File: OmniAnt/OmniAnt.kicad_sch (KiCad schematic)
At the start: 43 parts, among them J1 Connector, USB-TYPE-C-16P, J14 Conn_01x01, J15 Conn_01x01, J16 Conn_01x01, J17 Conn_01x01, J18 Conn_01x01, J19 Conn_01x01, J2 Conn_01x02_Pin, J20 Conn_01x01, J21 Conn_01x01, J22 Conn_01x01, J24 Conn_01x01, J3 Conn_01x04_Pin, J4 XT30PW-M, J5 XT30PW-M, J6 XT30PW-M, J7 XT30PW-M, U1 USBLC6-2P6, U2 TPSM53603RDA, U3 ESP32-S3-WROOM-1

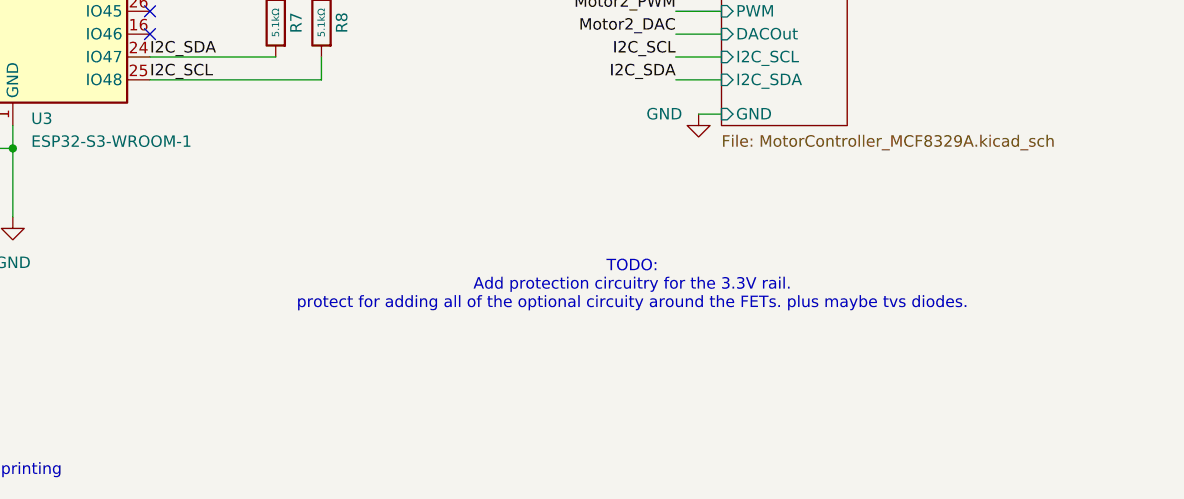
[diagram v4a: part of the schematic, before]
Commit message: Ok I did a lot of reading today. I'm going to split each FET into a sheet, so I can add the external circuitry more easily.
I may need to source a different FET. The one I selected has a good EAS, but the rating is only for 11A. and Ideally I would be able to do 19 or 20A. I'm sure I will never do that much current , but relying on the mosfet to handle things seems better than adding an additional tvs diode. Snubber is the way to go for sure to keep things cool.
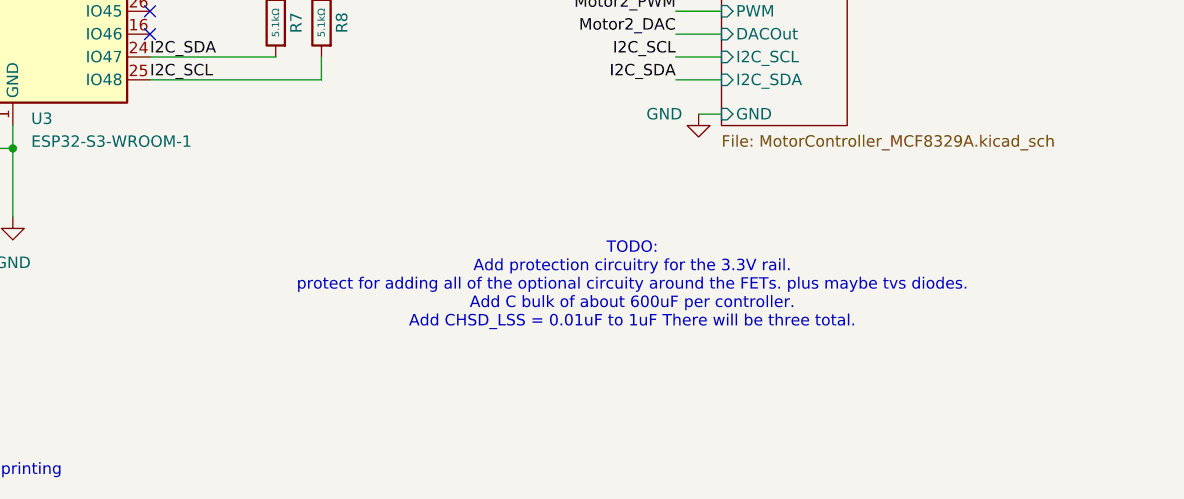
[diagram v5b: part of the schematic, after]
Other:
- note added: "TODO: Add protection circuitry for the 3.3V rail. protect for adding all of the optional circuity around the FETs. plus maybe tvs diodes. Add C bulk of about 600uF per controller. Add CHSD_LSS = 0.01uF to 1uF There will be three total."
- note removed: "TODO: Add protection circuitry for the 3.3V rail. protect for adding all of the optional circuity around the FETs. plus maybe tvs diodes."
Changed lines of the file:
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@@
 	(generator_version "9.0")
 	(paper "A4")
-	(text "TODO:\nAdd protection circuitry for the 3.3V rail. \nprotect for adding all of the optional circuity around the FETs. plus maybe tvs diodes. \n"
+	(text "TODO:\nAdd protection circuitry for the 3.3V rail. \nprotect for adding all of the optional circuity around the FETs. plus maybe tvs diodes. \nAdd C bulk of about 600uF per controller. \nAdd CHSD_LSS = 0.01uF to 1uF There will be three total. "
 		(exclude_from_sim yes)
 		(at 225.044 172.72 0)

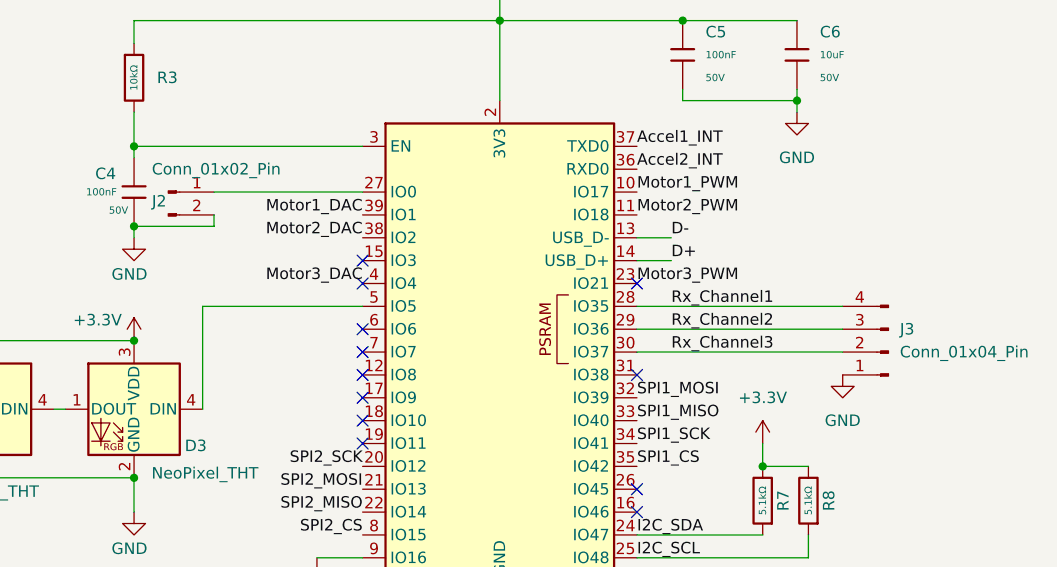
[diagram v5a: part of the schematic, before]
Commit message: I got the mosfets in as a separate sheet and selected the additional protection circuitry. I'm working on finding the other recommended capacitors now.
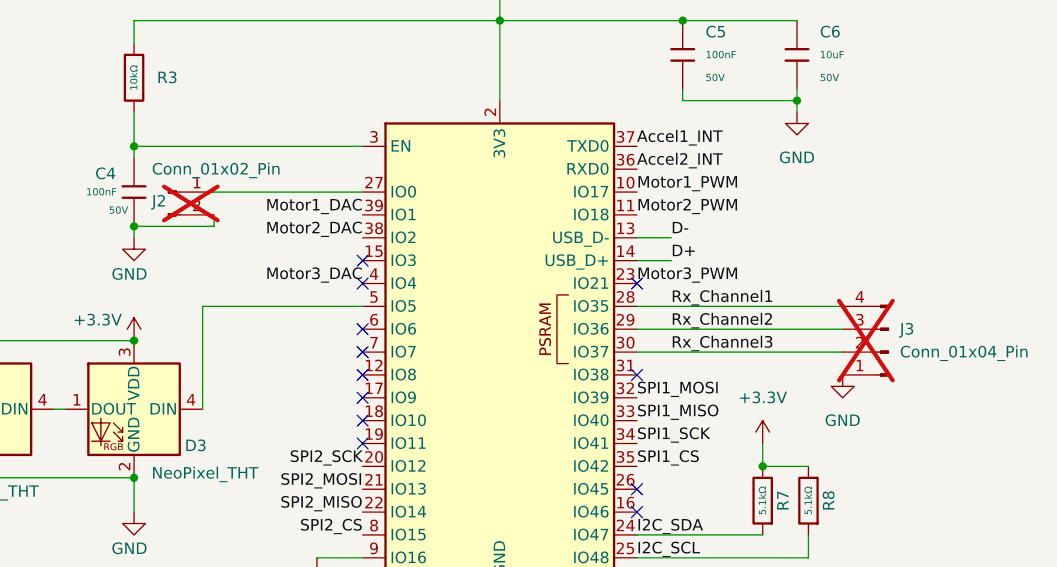
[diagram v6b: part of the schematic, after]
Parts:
- J2, J3: now not fitted
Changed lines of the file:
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@@
 		(in_bom yes)
 		(on_board yes)
-		(dnp no)
+		(dnp yes)
 		(fields_autoplaced yes)
 		(property "Reference" "J3"
@@
 		(in_bom yes)
 		(on_board yes)
-		(dnp no)
+		(dnp yes)
 		(property "Reference" "J2"
 			(at 118.364 110.236 0)

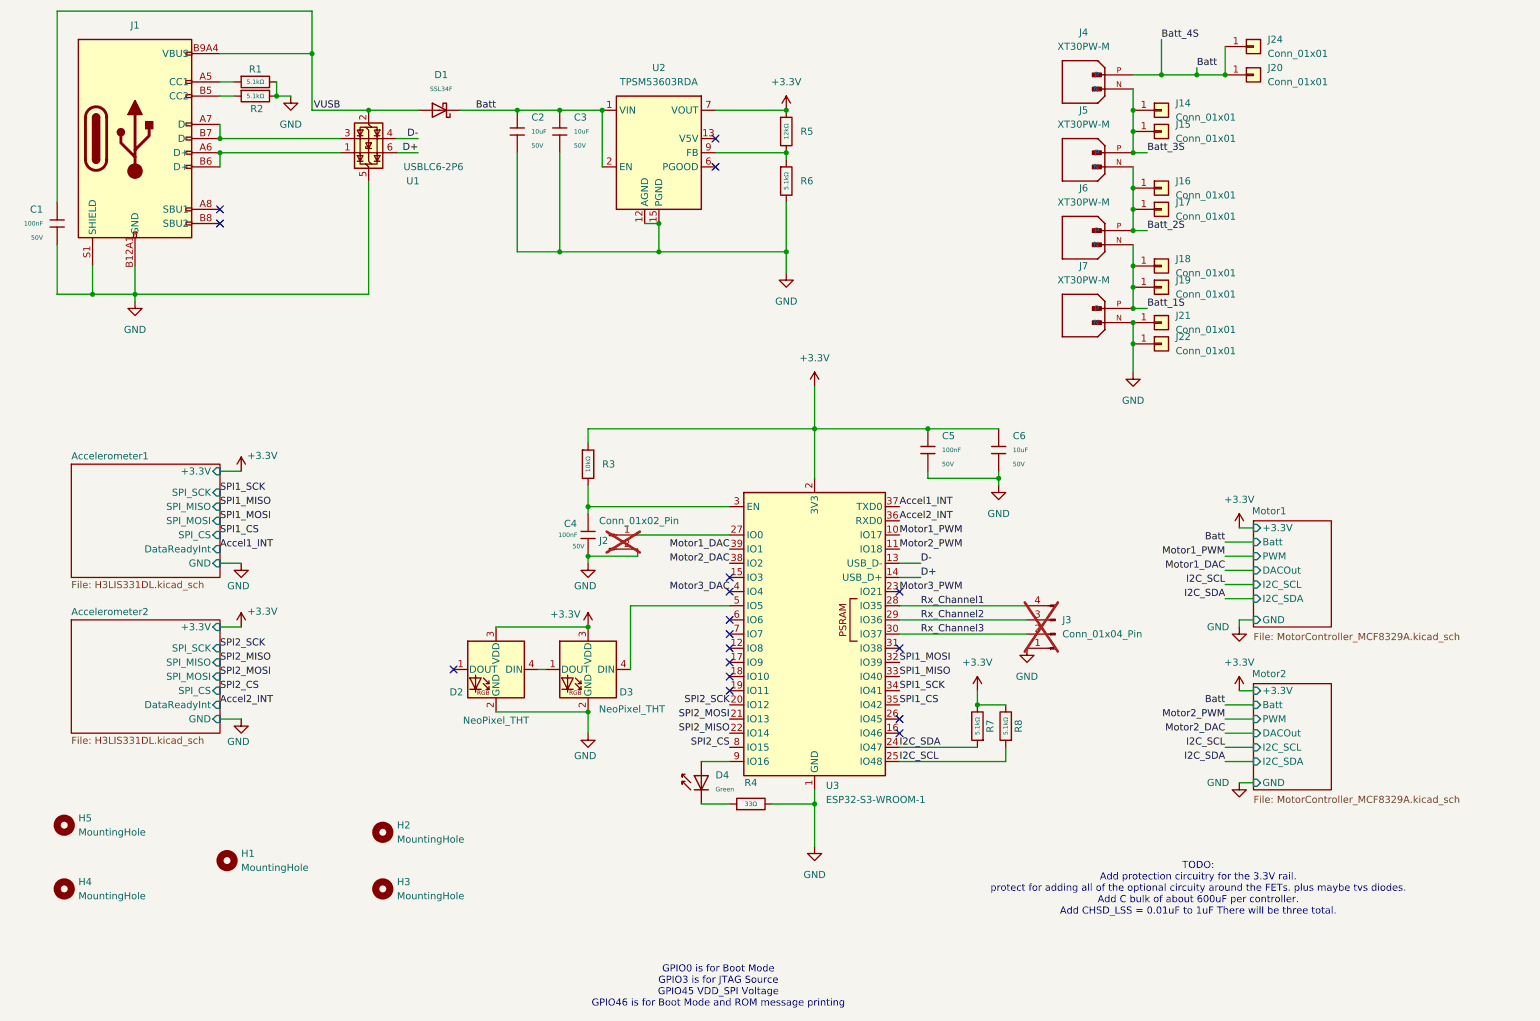
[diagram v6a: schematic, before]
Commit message: Well shit making the FETs into libraries totally screwed up the annotation :( I decided to just redo the layout for the FETs anyhow.
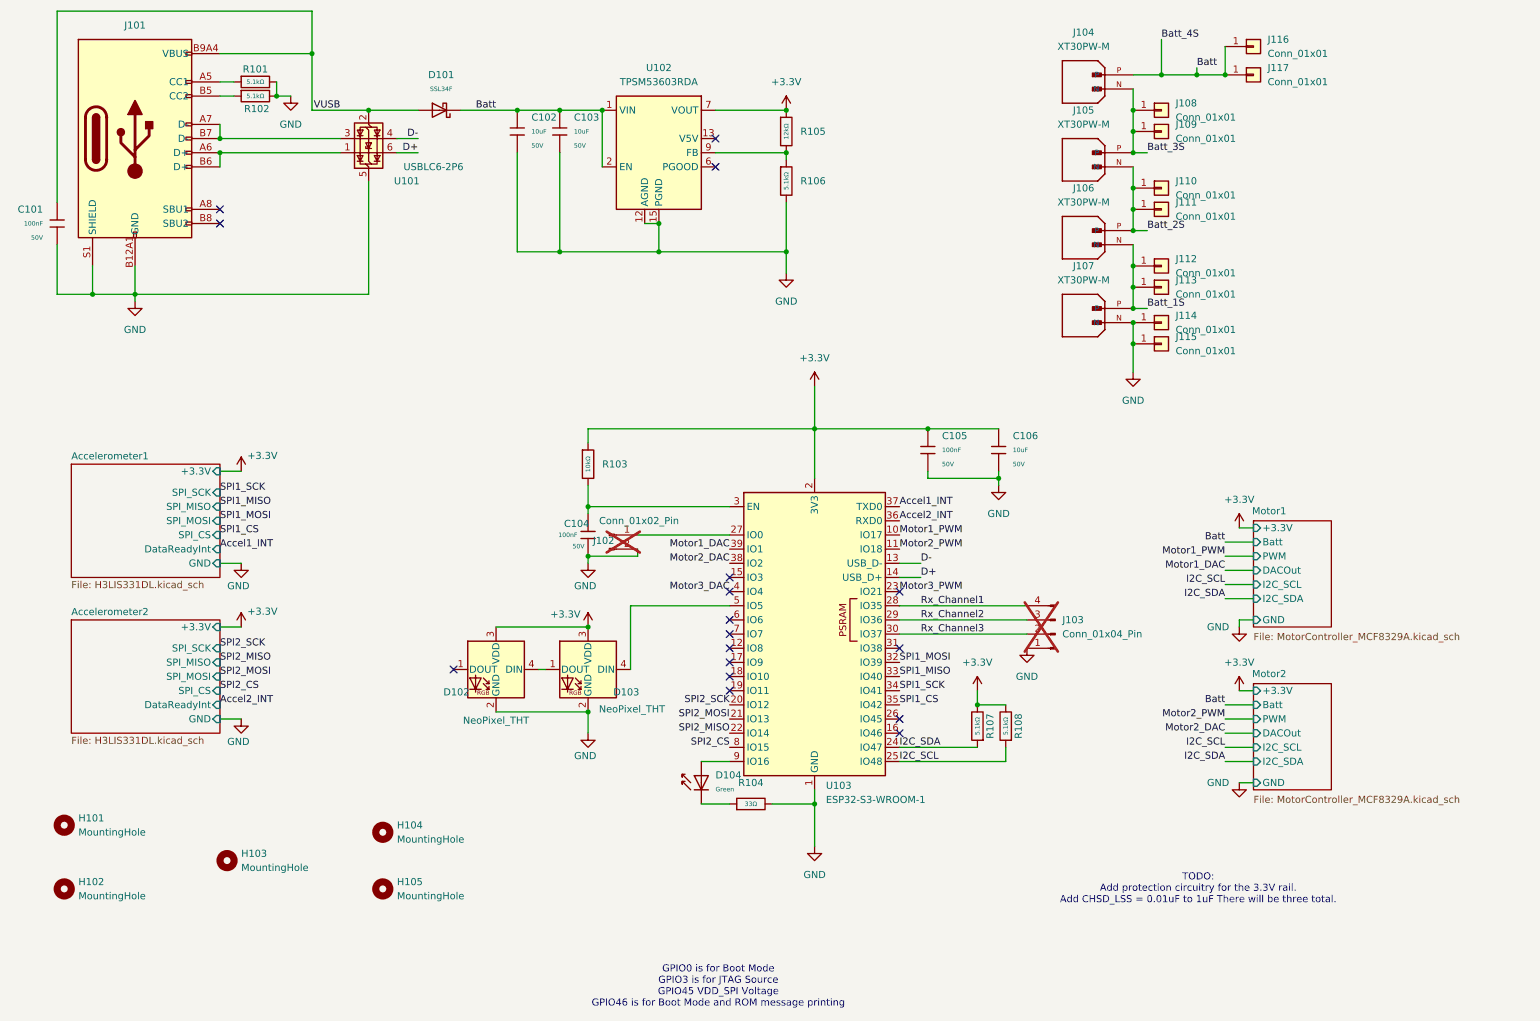
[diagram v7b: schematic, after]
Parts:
- C101: renamed from C1; Stock 58347526 -> 64667839
- C102: renamed from C2; Stock 1551376 -> 1647341
- C103: renamed from C3; Stock 1551376 -> 1647341
- C104: renamed from C4; Stock 58347526 -> 64667839
- C105: renamed from C5; Stock 58347526 -> 64667839
- C106: renamed from C6; Stock 1551376 -> 1647341
- D101: renamed from D1; Stock 1218 -> 1270
- D104: renamed from D4; Stock 2184914 -> 2276612
- R101: renamed from R1; Stock 4254023 -> 4532170
- R102: renamed from R2; Stock 4254023 -> 4532170
- R103: renamed from R3; Stock 16030120 -> 17848646
- R104: renamed from R4; Stock 2699126 -> 2828688
- R105: renamed from R5; Stock 515895 -> 586700
- R106: renamed from R6; Stock 4254023 -> 4532170
- R107: renamed from R7; Stock 4254023 -> 4532170
- R108: renamed from R8; Stock 4254023 -> 4532170
- renumbered D2 to D102, D3 to D103, H5 to H101, H4 to H102, H1 to H103, H2 to H104, H3 to H105, J1 to J101, J2 to J102, J3 to J103, J4 to J104, J5 to J105, J6 to J106, J7 to J107, J14 to J108, J15 to J109, J16 to J110, J17 to J111, J18 to J112, J19 to J113, J21 to J114, J22 to J115, J24 to J116, J20 to J117, U1 to U101, U2 to U102, U3 to U103
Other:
- note added: "TODO: Add protection circuitry for the 3.3V rail. Add CHSD_LSS = 0.01uF to 1uF There will be three total."
- note removed: "TODO: Add protection circuitry for the 3.3V rail. protect for adding all of the optional circuity around the FETs. plus maybe tvs diodes. Add C bulk of about 600uF per controller. Add CHSD_LSS = 0.01uF to 1uF There will be three total."

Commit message: Really good progress today. I got all the FETs placed again and routed. I'm working on the pours for the FETs now.
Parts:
- added C105, C106: 47uF, PCM_JLCPCB:C_1206, symbol PCM_JLCPCB-Capacitors:1206,47uF
- added D105: D_Zener, PCM_JLCPCB:D_SOD-123FL, symbol Device:D_Zener
- renumbered C105 to C107, C106 to C108
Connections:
- net +3.3V: now also C105.1, C106.1, D105.1 (K)
- net D+: now also U101.3 (I/O2); no longer U101.6 (I/O1)
- net D-: now also U101.1 (I/O1); no longer U101.4 (I/O2)
- net GND: now also U101.2 (GND), C105.2, C106.2, D105.2 (A); no longer U101.5 (VBUS)
- net VUSB: now also U101.5 (VBUS); no longer U101.2 (GND)
- net at J101.A6 (D+), J101.B6 (D+): now also U101.4 (I/O2); no longer U101.1 (I/O1)
- net at J101.A7 (D-), J101.B7 (D-): now also U101.6 (I/O1); no longer U101.3 (I/O2)
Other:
- note added: "TODO:"
- note removed: "TODO: Add protection circuitry for the 3.3V rail. Add CHSD_LSS = 0.01uF to 1uF There will be three total."
